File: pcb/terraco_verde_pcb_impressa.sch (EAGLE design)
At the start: 15 parts

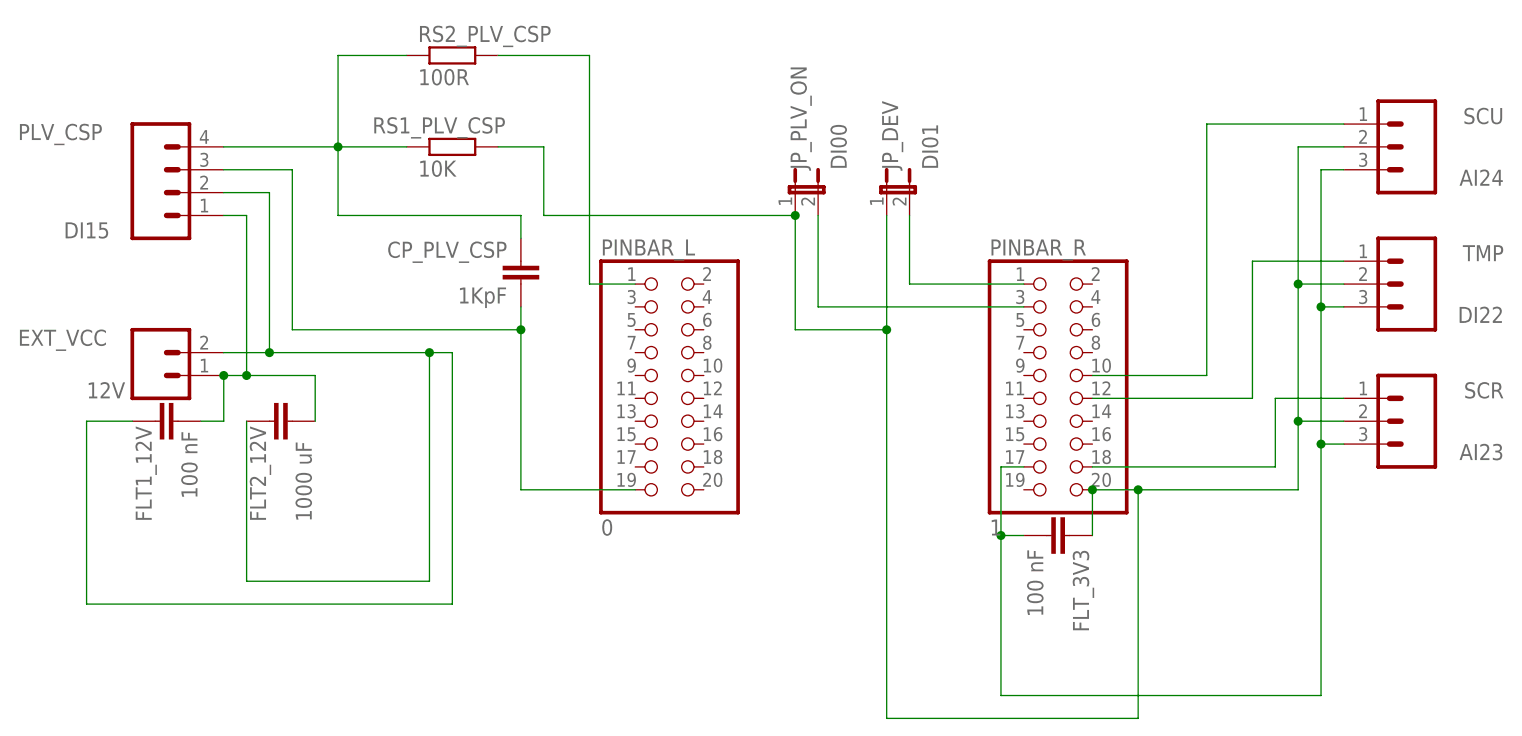
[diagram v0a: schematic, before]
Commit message: Alteração no projeto da PCB para incluir plano de terra e vias.
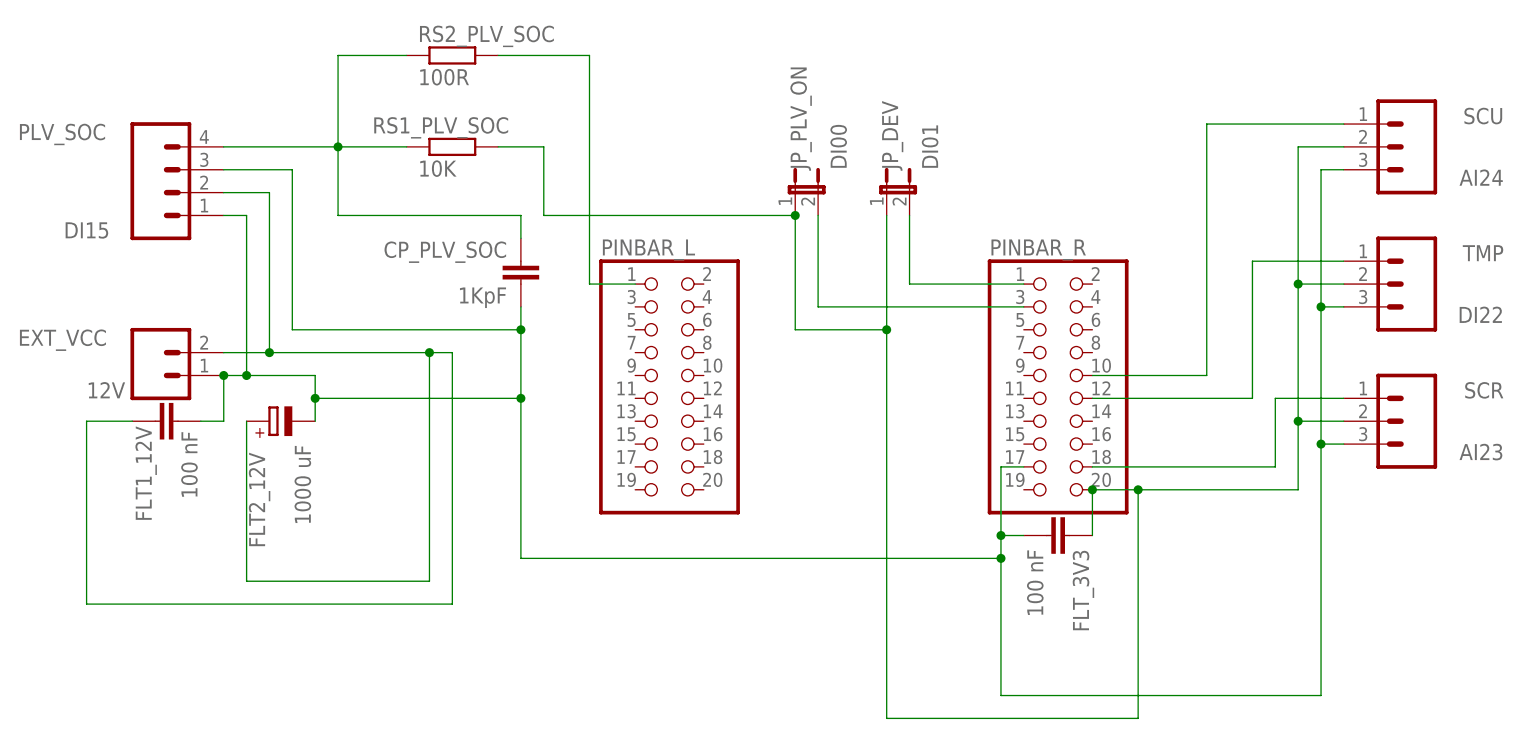
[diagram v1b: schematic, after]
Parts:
- FLT2_12V: device rcl:C-EU050-045X075 -> rcl:CPOL-EUE5-5
- renumbered CP_PLV_CSP to CP_PLV_SOC, PLV_CSP to PLV_SOC, RS1_PLV_CSP to RS1_PLV_SOC, RS2_PLV_CSP to RS2_PLV_SOC
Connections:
- net N$1 renamed VCC_3V3
- net N$10 renamed NDI15
- net N$11 renamed NDI22
- net N$12 renamed NAI24
- net N$13 renamed NDI15_2
- net N$6 renamed NAI23
- net N$7 renamed NDI01
- net N$8 renamed NDI00
- removed net N$2: FLT_3V3.2, PINBAR_R.17, SCR.3, SCU.3, TMP.3
- removed net N$3: EXT_VCC.1, FLT1_12V.2, FLT2_12V.2, PLV_SOC.1
- removed net N$4: CP_PLV_SOC.1, PINBAR_L.19, PLV_SOC.3
- removed net N$5: EXT_VCC.2, FLT1_12V.1, FLT2_12V.1, PLV_SOC.2
- new net GND: CP_PLV_SOC.1, EXT_VCC.1, FLT1_12V.2, FLT2_12V.-, FLT_3V3.2, PINBAR_R.17, PLV_SOC.1, PLV_SOC.3, SCR.3, SCU.3, TMP.3
- new net VCC_12V: EXT_VCC.2, FLT1_12V.1, FLT2_12V.+, PLV_SOC.2
